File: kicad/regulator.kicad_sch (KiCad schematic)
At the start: 15 parts, among them U1 LMR51450FNDRRR

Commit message: Miniaturizing the stepper drivers. They're still too big
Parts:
- C2, C3, C5, C6, C7: footprint Capacitor_SMD:C_0603_1608Metric -> Capacitor_SMD:C_0402_1005Metric
- R1, R2, R3, R4, R5: footprint Resistor_SMD:R_0603_1608Metric -> Resistor_SMD:R_0402_1005Metric
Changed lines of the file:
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@@
 			)
 		)
-		(property "Footprint" "Capacitor_SMD:C_0603_1608Metric"
+		(property "Footprint" "Capacitor_SMD:C_0402_1005Metric"
 			(at 100.0252 99.06 0)
 			(effects
@@
 			)
 		)
-		(property "Footprint" "Resistor_SMD:R_0603_1608Metric"
+		(property "Footprint" "Resistor_SMD:R_0402_1005Metric"
 			(at 216.662 93.98 90)
 			(effects
@@
 			)
 		)
-		(property "Footprint" "Resistor_SMD:R_0603_1608Metric"
+		(property "Footprint" "Resistor_SMD:R_0402_1005Metric"
 			(at 168.402 104.14 90)
 			(effects
@@
 			)
 		)
-		(property "Footprint" "Resistor_SMD:R_0603_1608Metric"
+		(property "Footprint" "Resistor_SMD:R_0402_1005Metric"
 			(at 205.232 106.68 90)
 			(effects
@@
 			)
 		)
-		(property "Footprint" "Capacitor_SMD:C_0603_1608Metric"
+		(property "Footprint" "Capacitor_SMD:C_0402_1005Metric"
 			(at 74.6252 99.06 0)
 			(effects
@@
 			)
 		)
-		(property "Footprint" "Capacitor_SMD:C_0603_1608Metric"
+		(property "Footprint" "Capacitor_SMD:C_0402_1005Metric"
 			(at 87.3252 99.06 0)
 			(effects
@@
 			)
 		)
-		(property "Footprint" "Resistor_SMD:R_0603_1608Metric"
+		(property "Footprint" "Resistor_SMD:R_0402_1005Metric"
 			(at 192.532 90.17 90)
 			(effects
@@
 			)
 		)
-		(property "Footprint" "Resistor_SMD:R_0603_1608Metric"
+		(property "Footprint" "Resistor_SMD:R_0402_1005Metric"
 			(at 205.232 93.98 90)
 			(effects
@@
 			)
 		)
-		(property "Footprint" "Capacitor_SMD:C_0603_1608Metric"
+		(property "Footprint" "Capacitor_SMD:C_0402_1005Metric"
 			(at 219.4052 109.22 0)
 			(effects
@@
 			)
 		)
-		(property "Footprint" "Capacitor_SMD:C_0603_1608Metric"
+		(property "Footprint" "Capacitor_SMD:C_0402_1005Metric"
 			(at 180.6448 93.98 0)
 			(effects

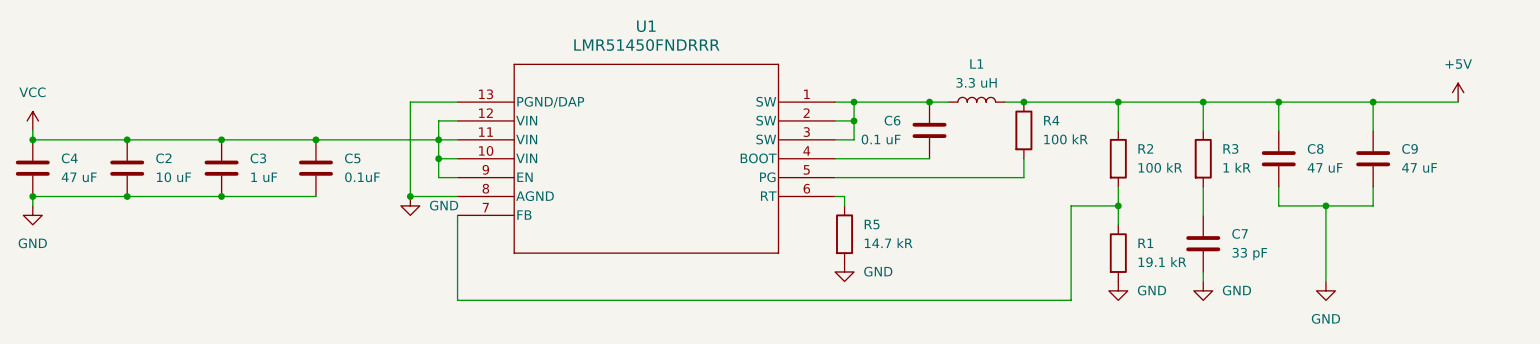
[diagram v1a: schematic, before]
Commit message: TMC2209->TMC2100, endstop protection optimization
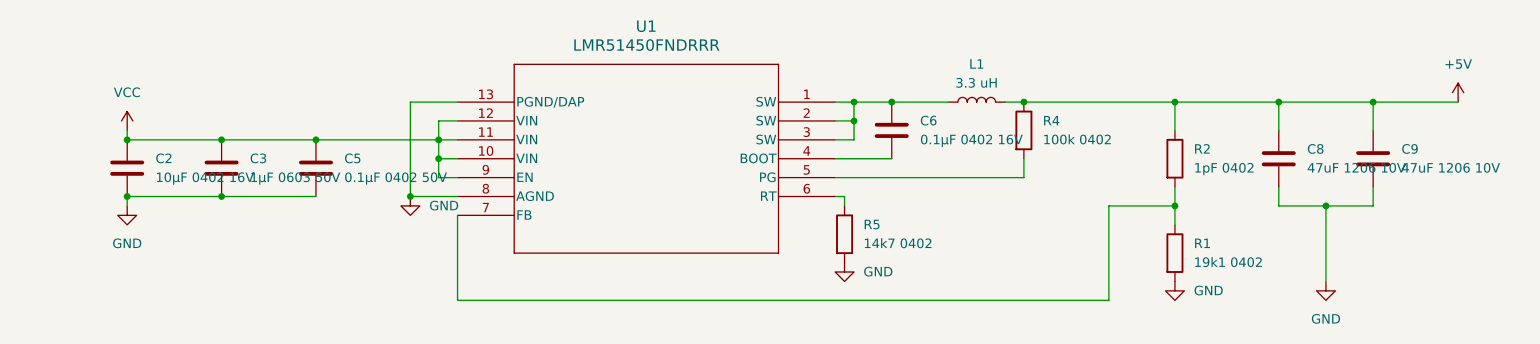
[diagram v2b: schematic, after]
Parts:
- removed C4: 47 uF, Capacitor_SMD:C_1206_3216Metric, symbol Device:C
- removed C7: 33 pF, Capacitor_SMD:C_0402_1005Metric, symbol Device:C
- removed R3: 1 kR, Resistor_SMD:R_0402_1005Metric, symbol Device:R
- C2: value 10 uF -> 10μF 0402 16V
- C3: value 1 uF -> 1μF 0603 50V
- C5: value 0.1uF -> 0.1μF 0402 50V
- C6: value 0.1 uF -> 0.1μF 0402 16V
- C8, C9: value 47 uF -> 47uF 1206 10V
- R1: value 19.1 kR -> 19k1 0402
- R2: value 100 kR -> 1pF 0402
- R4: value 100 kR -> 100k 0402
- R5: value 14.7 kR -> 14k7 0402
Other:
- moved on the sheet: C6, R1, R2

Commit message: new level shifter: bss138 transistors
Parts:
- C6: value 0.1μF 0402 16V -> 0.1μF 0603 16V
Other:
- moved on the sheet: R4
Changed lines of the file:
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@@
+	)
+	(junction
+		(at 199.39 86.36)
+		(diameter 0)
+		(color 0 0 0 0)
 	)
 	(junction
@@
 	)
 	(junction
-		(at 194.31 86.36)
-		(diameter 0)
-		(color 0 0 0 0)
-	)
-	(junction
 		(at 86.36 99.06)
 		(diameter 0)
@@
 	(wire
 		(pts
-			(xy 168.91 96.52) (xy 194.31 96.52)
+			(xy 168.91 96.52) (xy 199.39 96.52)
 		)
 		(stroke
@@
 	(wire
 		(pts
+			(xy 199.39 86.36) (xy 214.63 86.36)
+		)
+		(stroke
+			(width 0)
+			(type default)
+		)
+	)
+	(wire
+		(pts
 			(xy 118.11 113.03) (xy 118.11 101.6)
 		)
@@
 	(wire
 		(pts
-			(xy 194.31 96.52) (xy 194.31 93.98)
+			(xy 199.39 96.52) (xy 199.39 93.98)
 		)
 		(stroke
@@
 	(wire
 		(pts
-			(xy 194.31 86.36) (xy 214.63 86.36)
-		)
-		(stroke
-			(width 0)
-			(type default)
-		)
-	)
-	(wire
-		(pts
-			(xy 191.77 86.36) (xy 194.31 86.36)
+			(xy 191.77 86.36) (xy 199.39 86.36)
 		)
 		(stroke
@@
 	(symbol
 		(lib_id "Device:R")
-		(at 194.31 90.17 0)
+		(at 199.39 90.17 0)
 		(unit 1)
 		(exclude_from_sim no)
@@
 		(fields_autoplaced yes)
 		(property "Reference" "R4"
-			(at 196.85 88.9 0)
+			(at 201.93 88.9 0)
 			(effects
 				(font
@@
 		)
 		(property "Value" "100k 0402"
-			(at 196.85 91.44 0)
+			(at 201.93 91.44 0)
 			(effects
 				(font
@@
 		)
 		(property "Footprint" "Resistor_SMD:R_0402_1005Metric"
-			(at 192.532 90.17 90)
+			(at 197.612 90.17 90)
 			(effects
 				(font
@@
 		)
 		(property "Datasheet" "~"
-			(at 194.31 90.17 0)
+			(at 199.39 90.17 0)
 			(effects
 				(font
@@
 		)
 		(property "Description" ""
-			(at 194.31 90.17 0)
+			(at 199.39 90.17 0)
 			(effects
 				(font
@@
 			)
 		)
-		(property "Value" "0.1μF 0402 16V"
+		(property "Value" "0.1μF 0603 16V"
 			(at 180.34 91.44 0)
 			(effects

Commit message: layout progress
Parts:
- U1: footprint rephat-parts:WSON_SDRRR_TEX -> WSON_SDRRR_TEX
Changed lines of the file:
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@@
 			)
 		)
-		(property "Footprint" "rephat-parts:WSON_SDRRR_TEX"
+		(property "Footprint" "WSON_SDRRR_TEX"
 			(at 143.51 95.25 0)
 			(effects
@@
 			)
 		)
-		(property "Description" ""
+		(property "Description" "Unpolarized capacitor"
 			(at 99.06 95.25 0)
 			(effects
@@
 			)
 		)
-		(property "Description" ""
+		(property "Description" "Inductor"
 			(at 187.96 86.36 0)
 			(effects
@@
 			)
 		)
-		(property "Description" ""
+		(property "Description" "Resistor"
 			(at 170.18 104.14 0)
 			(effects
@@
 			)
 		)
-		(property "Description" ""
+		(property "Description" "Resistor"
 			(at 214.63 106.68 0)
 			(effects
@@
 			)
 		)
-		(property "Description" ""
+		(property "Description" "Unpolarized capacitor"
 			(at 73.66 95.25 0)
 			(effects
@@
 			)
 		)
-		(property "Description" ""
+		(property "Description" "Power symbol creates a global label with name \"GND\" , ground"
 			(at 73.66 100.33 0)
 			(effects
@@
 			)
 		)
-		(property "Description" ""
+		(property "Description" "Power symbol creates a global label with name \"GND\" , ground"
 			(at 214.63 110.49 0)
 			(effects
@@
 			)
 		)
-		(property "Description" ""
+		(property "Description" "Unpolarized capacitor"
 			(at 86.36 95.25 0)
 			(effects
@@
 			)
 		)
-		(property "Datasheet" "https://www.we-online.com/components/products/datasheet/885012108012.pdf"
+		(property "Datasheet" "~"
 			(at 241.3 93.98 0)
 			(effects
@@
 			)
 		)
-		(property "Description" ""
+		(property "Description" "Unpolarized capacitor"
 			(at 241.3 93.98 0)
 			(effects
@@
 			)
 		)
-		(property "Description" ""
+		(property "Description" "Resistor"
 			(at 199.39 90.17 0)
 			(effects
@@
 			)
 		)
-		(property "Description" ""
+		(property "Description" "Power symbol creates a global label with name \"VCC\""
 			(at 73.66 90.17 0)
 			(effects
@@
 			)
 		)
-		(property "Description" ""
+		(property "Description" "Resistor"
 			(at 214.63 93.98 0)
 			(effects
@@
 			)
 		)
-		(property "Description" ""
+		(property "Description" "Power symbol creates a global label with name \"GND\" , ground"
 			(at 111.76 99.06 0)
 			(effects
@@
 			)
 		)
-		(property "Description" ""
+		(property "Description" "Power symbol creates a global label with name \"GND\" , ground"
 			(at 234.95 110.49 0)
 			(effects
@@
 			)
 		)
-		(property "Description" ""
+		(property "Description" "Power symbol creates a global label with name \"GND\" , ground"
 			(at 170.18 107.95 0)
 			(effects
@@
 			)
 		)
-		(property "Description" ""
+		(property "Description" "Power symbol creates a global label with name \"+5V\""
 			(at 252.73 86.36 0)
 			(effects
@@
 			)
 		)
-		(property "Description" ""
+		(property "Description" "Unpolarized capacitor"
 			(at 176.53 90.17 0)
 			(effects
@@
 			)
 		)
-		(property "Datasheet" "https://www.we-online.com/components/products/datasheet/885012108012.pdf"
+		(property "Datasheet" "~"
 			(at 228.6 93.98 0)
 			(effects
@@
 			)
 		)
-		(property "Description" ""
+		(property "Description" "Unpolarized capacitor"
 			(at 228.6 93.98 0)
 			(effects
